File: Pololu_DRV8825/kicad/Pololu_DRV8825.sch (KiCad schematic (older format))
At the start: 30 parts, among them J1 CONN_02X03, J2 CONN_01X02, J3 CONN_01X02, P1 CONN_01X10, P2 CONN_01X10, P3 CONN_01X10, P4 CONN_01X04, P5 CONN_01X04, U1 MSP430G2553IN20, U2 LM2931Z-3.3/5.0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

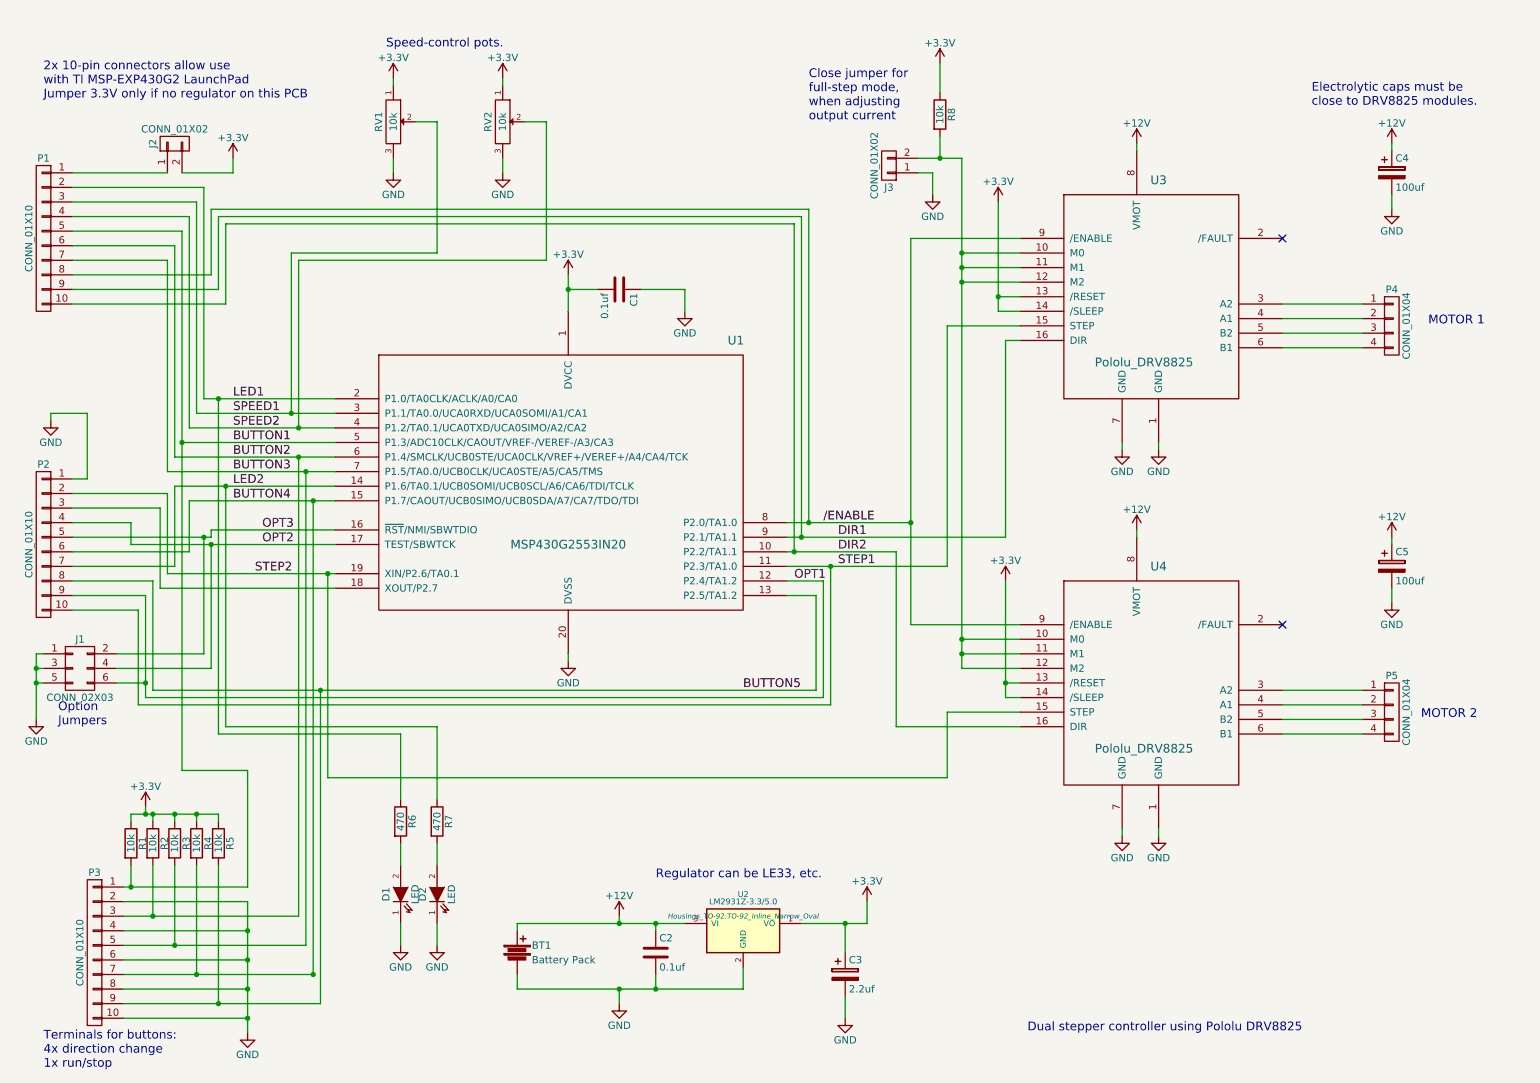
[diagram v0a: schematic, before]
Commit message: DRV8825 - parts placed
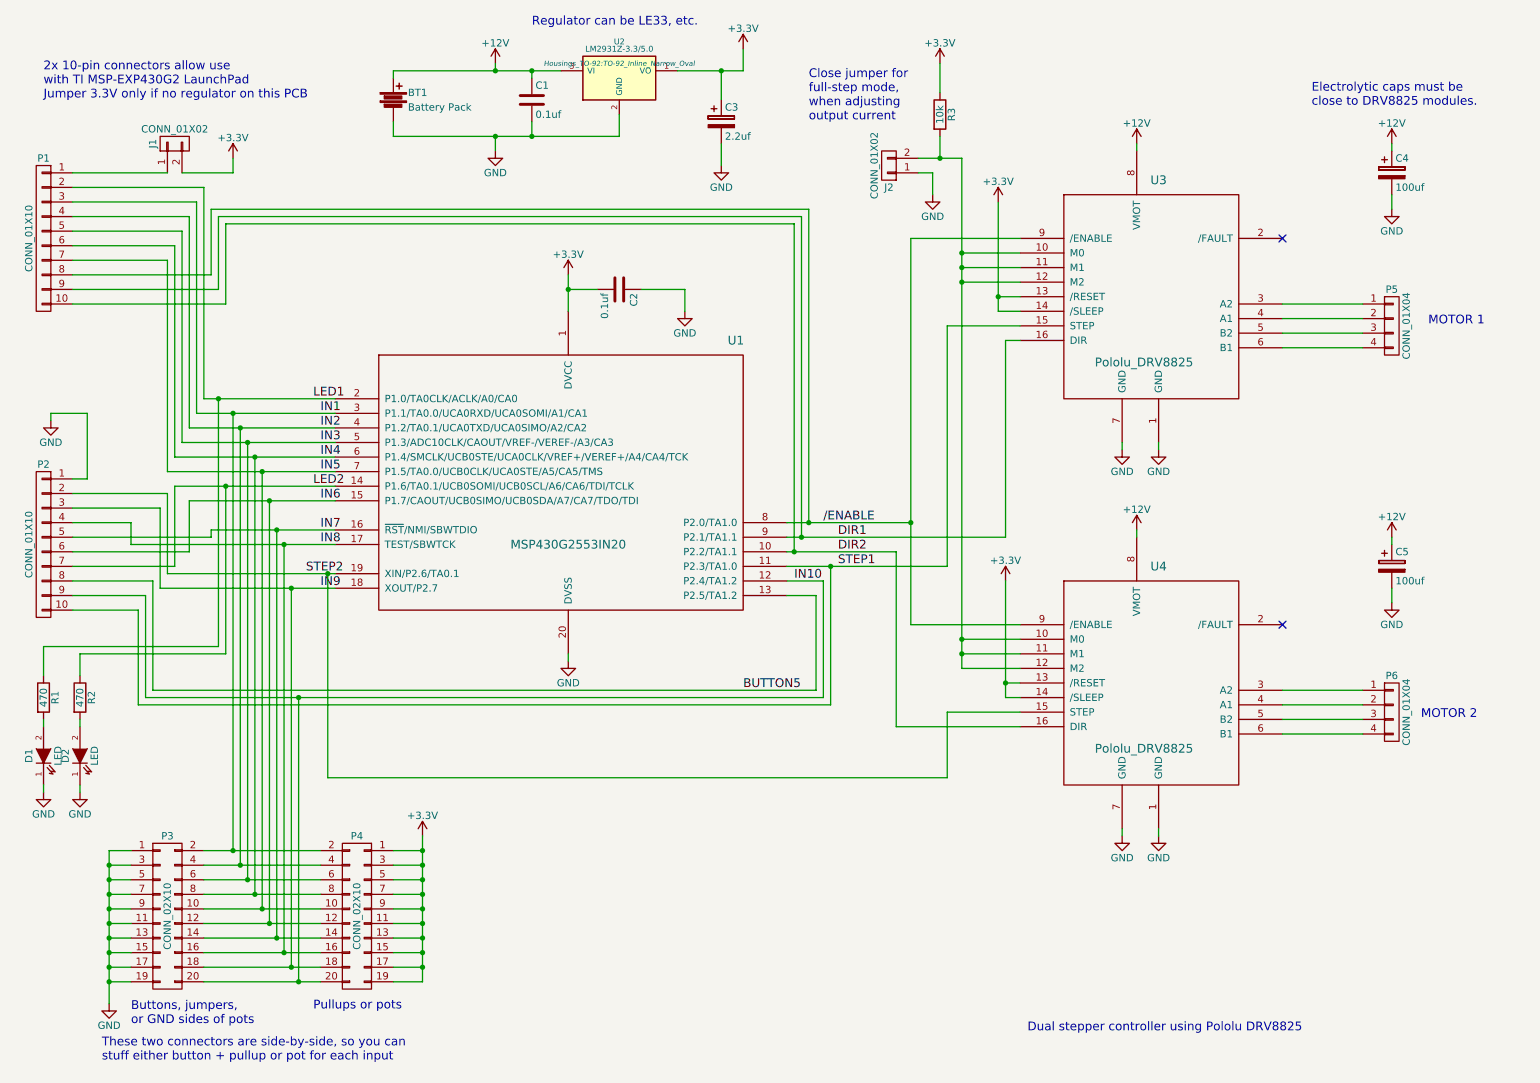
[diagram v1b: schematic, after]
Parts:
- removed J1: CONN_02X03, Pin_Headers:Pin_Header_Angled_2x03, symbol CONN_02X03
- removed P3: CONN_01X10, Pin_Headers:Pin_Header_Angled_1x10, symbol CONN_01X10
- removed R1, R2, R3, R4, R5: 10k, Resistors_ThroughHole:Resistor_Horizontal_RM15mm, symbol R
- removed RV1, RV2: 10k, Pin_Headers:Pin_Header_Straight_1x03, symbol POT
- added P3, P4: CONN_02X10, Pin_Headers:Pin_Header_Straight_2x10, symbol CONN_02X10
- C3: footprint Capacitors_SMD:C_1206_HandSoldering -> Capacitors_ThroughHole:C_Disc_D3_P2.5
- D1, D2: footprint LEDs:LED-1206 -> LEDs:LED-3MM
- J1: renamed from J2; footprint Pin_Headers:Pin_Header_Angled_1x02 -> Pin_Headers:Pin_Header_Straight_1x02
- J2: renamed from J3; footprint Pin_Headers:Pin_Header_Angled_1x02 -> Pin_Headers:Pin_Header_Straight_1x02
- P1, P2: footprint Pin_Headers:Pin_Header_Angled_1x10 -> Pin_Headers:Pin_Header_Straight_1x10
- P5: renamed from P4; footprint Pin_Headers:Pin_Header_Angled_1x04 -> Pin_Headers:Pin_Header_Straight_1x04
- P6: renamed from P5; footprint Pin_Headers:Pin_Header_Angled_1x04 -> Pin_Headers:Pin_Header_Straight_1x04
- renumbered C2 to C1, C1 to C2, R6 to R1, R7 to R2, R8 to R3
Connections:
- net +3V3: now also P4.1 (P1), P4.11 (P11), P4.13 (P13), P4.15 (P15), P4.17 (P17), P4.19 (P19), P4.3 (P3), P4.5 (P5), P4.7 (P7), P4.9 (P9)
- net GND: now also P3.1 (P1), P3.11 (P11), P3.13 (P13), P3.15 (P15), P3.17 (P17), P3.19 (P19), P3.3 (P3), P3.5 (P5), P3.7 (P7), P3.9 (P9)
- net IN9: now reaches P2.3 (P3), U1.18 (XOUT/P2.7)
- net IN9: now also P3.18 (P18), P4.18 (P18)
- net BUTTON1 renamed IN3
- net IN3: now also P3.6 (P6), P4.6 (P6)
- net BUTTON2 renamed IN4
- net IN4: now also P3.8 (P8), P4.8 (P8)
- net BUTTON3 renamed IN5
- net IN5: now also P3.10 (P10), P4.10 (P10)
- net BUTTON4 renamed IN6
- net IN6: now also P3.12 (P12), P4.12 (P12)
- net OPT1 renamed IN10
- net IN10: now also P3.20 (P20), P4.20 (P20)
- net OPT2 renamed IN8
- net IN8: now also P3.16 (P16), P4.16 (P16)
- net OPT3 renamed IN7
- net IN7: now also P3.14 (P14), P4.14 (P14)
- net SPEED1 renamed IN1
- net IN1: now also P3.2 (P2), P4.2 (P2)
- net SPEED2 renamed IN2
- net IN2: now also P3.4 (P4), P4.4 (P4)
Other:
- note added: "Buttons, jumpers,\nor GND sides of pots"
- note added: "Pullups or pots"
- note added: "These two connectors are side-by-side, so you can\nstuff either button + pullup or pot for each input"
- note removed: "Option\nJumpers"
- note removed: "Speed-control pots."
- note removed: "Terminals for buttons:\n4x direction change\n1x run/stop"
- moved on the sheet: BT1, C1, C3, D1, D2, R1, R2, U2

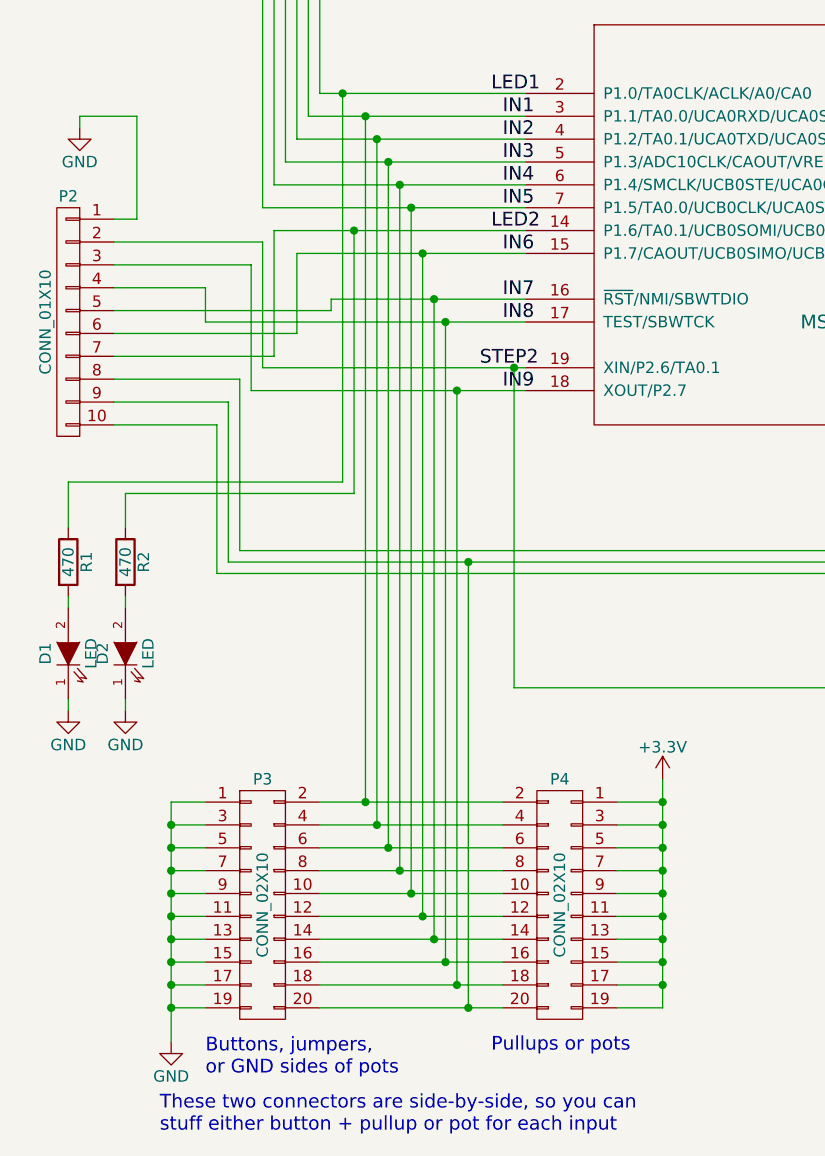
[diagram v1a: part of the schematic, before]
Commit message: DRV8825 first routed board with mounting holes
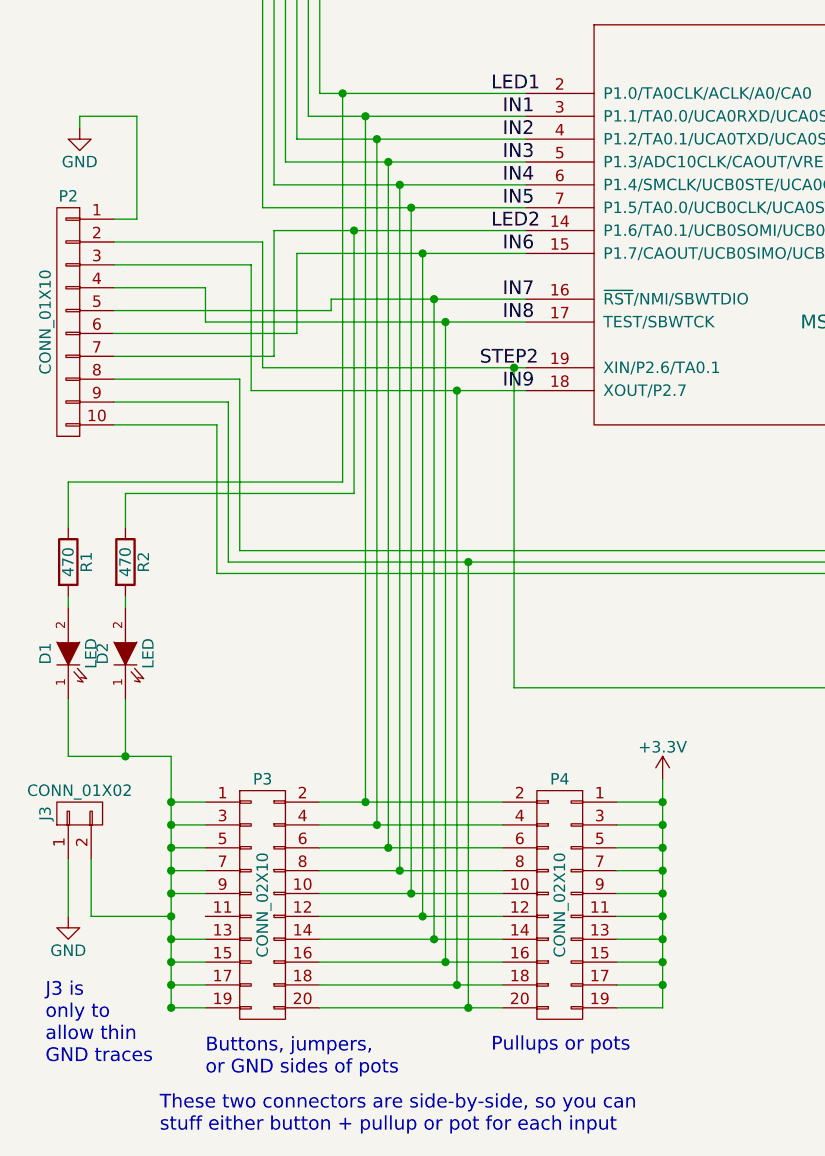
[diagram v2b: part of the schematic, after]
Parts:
- added J3: CONN_01X02, Pin_Headers:Pin_Header_Straight_1x02, symbol CONN_01X02
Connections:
- net GND: now also J3.1 (P1); no longer D1.1 (K), D2.1 (K), P3.1 (P1), P3.11 (P11), P3.13 (P13), P3.15 (P15), P3.17 (P17), P3.19 (P19), P3.3 (P3), P3.5 (P5), P3.7 (P7), P3.9 (P9)
- new net: D1.1 (K), D2.1 (K), J3.2 (P2), P3.1 (P1), P3.13 (P13), P3.15 (P15), P3.17 (P17), P3.19 (P19), P3.3 (P3), P3.5 (P5), P3.7 (P7), P3.9 (P9)
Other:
- note added: "J3 is\nonly to\nallow thin\nGND traces"
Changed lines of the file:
@@
-$EndComp
-$Comp
-L GND #PWR023
-U 1 1 55E88C76
-P 700 5850
-F 0 "#PWR023" H 700 5600 50  0001 C CNN
-F 1 "GND" H 700 5700 50  0000 C CNN
-F 2 "" H 700 5850 60  0000 C CNN
-F 3 "" H 700 5850 60  0000 C CNN
-	1    700  5850
-	1    0    0    -1
-$EndComp
-$Comp
-L GND #PWR024
-U 1 1 55E88CD5
-P 950 5850
-F 0 "#PWR024" H 950 5600 50  0001 C CNN
-F 1 "GND" H 950 5700 50  0000 C CNN
-F 2 "" H 950 5850 60  0000 C CNN
-F 3 "" H 950 5850 60  0000 C CNN
-	1    950  5850
-	1    0    0    -1
 $EndComp
 $Comp
@@
 $EndComp
 $Comp
-L GND #PWR026
-U 1 1 55E9D8EE
-P 1150 7300
-F 0 "#PWR026" H 1150 7050 50  0001 C CNN
-F 1 "GND" H 1150 7150 50  0000 C CNN
-F 2 "" H 1150 7300 60  0000 C CNN
-F 3 "" H 1150 7300 60  0000 C CNN
-	1    1150 7300
-	1    0    0    -1
-$EndComp
-$Comp
 L CONN_02X10 P4
 U 1 1 55EA0321
@@
 $EndComp
 $Comp
-L +3.3V #PWR027
+L +3.3V #PWR026
 U 1 1 55EA1205
 P 3300 6150
-F 0 "#PWR027" H 3300 6000 50  0001 C CNN
+F 0 "#PWR026" H 3300 6000 50  0001 C CNN
 F 1 "+3.3V" H 3300 6290 50  0000 C CNN
 F 2 "" H 3300 6150 60  0000 C CNN
@@
 	1700 1900 900  1900
 Wire Wire Line
-	2700 3450 1650 3450
+	1650 3450 2700 3450
 Wire Wire Line
 	1650 2000 900  2000
@@
 	1850 4050 2700 4050
 Wire Wire Line
-	2700 4150 1300 4150
+	1300 4150 2700 4150
 Wire Wire Line
 	1300 4150 1300 4000
@@
 	1300 6250 1150 6250
 Wire Wire Line
-	1150 6250 1150 7300
-Wire Wire Line
 	1300 6350 1150 6350
 Connection ~ 1150 6350
 Wire Wire Line
-	1300 6450 1150 6450
+	1150 6450 1300 6450
 Connection ~ 1150 6450
 Wire Wire Line
-	1300 6550 1150 6550
+	1150 6550 1300 6550
 Connection ~ 1150 6550
 Wire Wire Line
-	1300 6650 1150 6650
+	1150 6650 1300 6650
 Connection ~ 1150 6650
 Wire Wire Line
-	1300 6750 1150 6750
+	800  6750 1150 6750
 Connection ~ 1150 6750
 Wire Wire Line
-	1300 6850 1150 6850
+	1150 6850 1300 6850
 Connection ~ 1150 6850
 Wire Wire Line
-	1300 6950 1150 6950
+	1150 6950 1300 6950
 Connection ~ 1150 6950
 Wire Wire Line
-	1300 7050 1150 7050
+	1150 7050 1300 7050
 Connection ~ 1150 7050
 Wire Wire Line
-	1300 7150 1150 7150
+	1150 7150 1300 7150
 Connection ~ 1150 7150
 Wire Wire Line
@@
 Connection ~ 2450 5200
 Wire Wire Line
-	3100 7150 3300 7150
-Wire Wire Line
-	3300 7150 3300 6150
+	3300 7150 3100 7150
+Wire Wire Line
+	3300 6150 3300 7150
 Wire Wire Line
 	3100 7050 3300 7050
@@
 These two connectors are side-by-side, so you can\nstuff either button + pullup or pot for each input
 Wire Wire Line
-	700  5850 700  5800
-Wire Wire Line
-	950  5850 950  5800
+	700  5800 700  6050
+Wire Wire Line
+	950  5800 950  6050
+$Comp
+L CONN_01X02 J3
+U 1 1 55E9E66F
+P 750 6300
+F 0 "J3" H 750 6450 50  0000 C CNN
+F 1 "CONN_01X02" V 850 6300 50  0000 C CNN
+F 2 "Pin_Headers:Pin_Header_Straight_1x02" H 750 6300 60  0001 C CNN
+F 3 "" H 750 6300 60  0000 C CNN
+	1    750  6300
+	0    -1   -1   0
+$EndComp
+Wire Wire Line
+	1150 6050 1150 7150
+Wire Wire Line
+	800  6500 800  6750
+$Comp
+L GND #PWR027
+U 1 1 55E9E96F
+P 700 6750
+F 0 "#PWR027" H 700 6500 50  0001 C CNN
+F 1 "GND" H 700 6600 50  0000 C CNN
+F 2 "" H 700 6750 60  0000 C CNN
+F 3 "" H 700 6750 60  0000 C CNN
+	1    700  6750
+	1    0    0    -1
+$EndComp
+Wire Wire Line
+	700  6500 700  6750
+Text Notes 600  7400 0    60   ~ 0
+J3 is\nonly to\nallow thin\nGND traces
+Wire Wire Line
+	700  6050 1150 6050
+Connection ~ 1150 6250
+Connection ~ 950  6050
 $EndSCHEMATC

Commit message: Ready for first manufacturing run
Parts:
- added Hole1, Hole2, Hole3, Hole4: MountingHole, Connect:1pin, symbol MountingHole
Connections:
- net at D1.1 (K), D2.1 (K), J3.2 (P2)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: now also P3.11 (P11)
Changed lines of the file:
@@
 $EndComp
 $Comp
-L GND #PWR025
+L GND #PWR023
 U 1 1 55E92FCD
 P 5100 2550
-F 0 "#PWR025" H 5100 2300 50  0001 C CNN
+F 0 "#PWR023" H 5100 2300 50  0001 C CNN
 F 1 "GND" H 5100 2400 50  0000 C CNN
 F 2 "" H 5100 2550 60  0000 C CNN
@@
 $EndComp
 $Comp
-L +3.3V #PWR026
+L +3.3V #PWR024
 U 1 1 55EA1205
 P 3300 6150
-F 0 "#PWR026" H 3300 6000 50  0001 C CNN
+F 0 "#PWR024" H 3300 6000 50  0001 C CNN
 F 1 "+3.3V" H 3300 6290 50  0000 C CNN
 F 2 "" H 3300 6150 60  0000 C CNN
@@
 Connection ~ 1150 6650
 Wire Wire Line
-	800  6750 1150 6750
+	800  6750 1300 6750
 Connection ~ 1150 6750
 Wire Wire Line
@@
 	800  6500 800  6750
 $Comp
-L GND #PWR027
+L GND #PWR025
 U 1 1 55E9E96F
 P 700 6750
-F 0 "#PWR027" H 700 6500 50  0001 C CNN
+F 0 "#PWR025" H 700 6500 50  0001 C CNN
 F 1 "GND" H 700 6600 50  0000 C CNN
 F 2 "" H 700 6750 60  0000 C CNN
@@
 Connection ~ 1150 6250
 Connection ~ 950  6050
+$Comp
+L MountingHole Hole1
+U 1 1 55E9FF79
+P 4250 6550
+F 0 "Hole1" H 4250 6550 60  0000 C CNN
+F 1 "MountingHole" H 4250 6550 60  0000 C CNN
+F 2 "Connect:1pin" H 4250 6550 60  0001 C CNN
+F 3 "" H 4250 6550 60  0000 C CNN
+	1    4250 6550
+	1    0    0    -1
+$EndComp
+$Comp
+L MountingHole Hole3
+U 1 1 55E9FFFF
+P 4900 6550
+F 0 "Hole3" H 4900 6550 60  0000 C CNN
+F 1 "MountingHole" H 4900 6550 60  0000 C CNN
+F 2 "Connect:1pin" H 4900 6550 60  0001 C CNN
+F 3 "" H 4900 6550 60  0000 C CNN
+	1    4900 6550
+	1    0    0    -1
+$EndComp
+$Comp
+L MountingHole Hole2
+U 1 1 55EA0073
+P 4250 7200
+F 0 "Hole2" H 4250 7200 60  0000 C CNN
+F 1 "MountingHole" H 4250 7200 60  0000 C CNN
+F 2 "Connect:1pin" H 4250 7200 60  0001 C CNN
+F 3 "" H 4250 7200 60  0000 C CNN
+	1    4250 7200
+	1    0    0    -1
+$EndComp
+$Comp
+L MountingHole Hole4
+U 1 1 55EA00FC
+P 4900 7200
+F 0 "Hole4" H 4900 7200 60  0000 C CNN
+F 1 "MountingHole" H 4900 7200 60  0000 C CNN
+F 2 "Connect:1pin" H 4900 7200 60  0001 C CNN
+F 3 "" H 4900 7200 60  0000 C CNN
+	1    4900 7200
+	1    0    0    -1
+$EndComp
 $EndSCHEMATC
